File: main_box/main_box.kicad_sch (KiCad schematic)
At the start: 0 parts

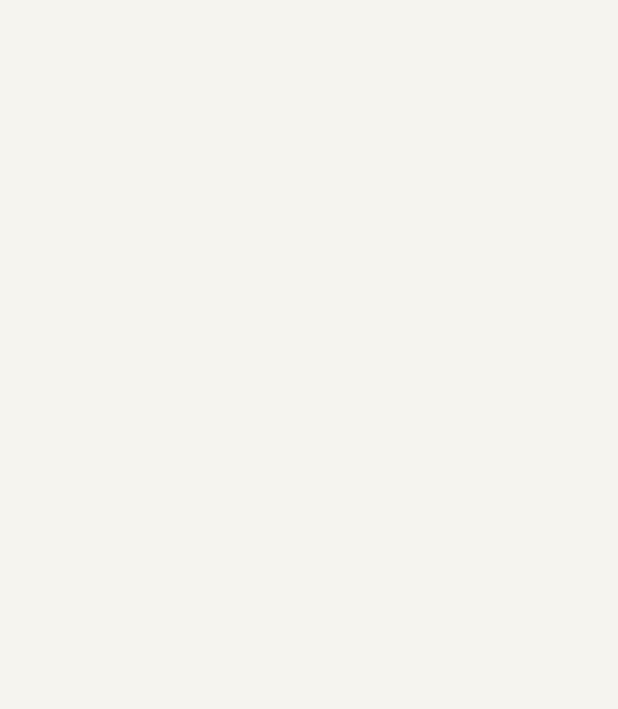
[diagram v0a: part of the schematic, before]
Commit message: Added 5v pówer supply for independent raspberry pi power, modified the switchgear topology
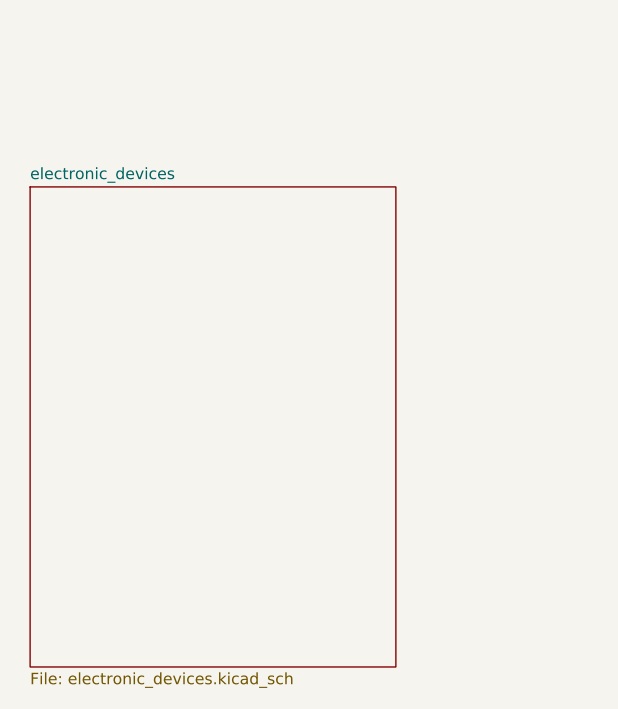
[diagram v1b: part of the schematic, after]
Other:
- added sheet electronic_devices (electronic_devices.kicad_sch)
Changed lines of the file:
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@@
+    )
+  )
+  (sheet (at 22.86 102.87) (size 40.64 53.34) (fields_autoplaced)
+    (stroke (width 0.1524) (type solid) (color 0 0 0 0))
+    (fill (color 0 0 0 0.0000))
+    (property "Sheet name" "electronic_devices" (id 0) (at 22.86 102.1584 0)
+      (effects (font (size 1.27 1.27)) (justify left bottom))
+    )
+    (property "Sheet file" "electronic_devices.kicad_sch" (id 1) (at 22.86 156.7946 0)
+      (effects (font (size 1.27 1.27)) (justify left top))
     )
   )
@@
     (path "/7bafe9bc-eba9-4810-a855-8b4f34bb53ef" (page "3"))
     (path "/63d2de20-f243-448e-8f9b-9238fd5af361" (page "4"))
+    (path "/eb51af8c-f931-4087-841b-b930618e5f3f" (page "5"))
+  )
+  (symbol_instances
+    (path "/63d2de20-f243-448e-8f9b-9238fd5af361/2175fe63-e824-4590-bc28-3e8589ee19d9"
+      (reference "#PWR?") (unit 1) (value "+48V") (footprint "")
+    )
+    (path "/997c2f12-73ba-4c01-9ee0-42e37cbab790/4d0b4730-b3d1-43cb-accd-4cc79974c8c5"
+      (reference "#PWR?") (unit 1) (value "AC") (footprint "")
+    )
+    (path "/63d2de20-f243-448e-8f9b-9238fd5af361/68c81a5f-fa55-4394-b81b-8e4332a2bcfc"
+      (reference "#PWR?") (unit 1) (value "GND") (footprint "")
+    )
+    (path "/63d2de20-f243-448e-8f9b-9238fd5af361/726d0c38-9170-4a3a-b0d1-f86487597b7c"
+      (reference "#PWR?") (unit 1) (value "~") (footprint "")
+    )
+    (path "/997c2f12-73ba-4c01-9ee0-42e37cbab790/8dd2ebd0-beab-4a6a-a970-4109d2d0d2a4"
+      (reference "#PWR?") (unit 1) (value "+48V") (footprint "")
+    )
+    (path "/997c2f12-73ba-4c01-9ee0-42e37cbab790/c7b12abe-ed41-4f50-ac10-dd4835ba4d6b"
+      (reference "#PWR?") (unit 1) (value "NEUT") (footprint "")
+    )
+    (path "/63d2de20-f243-448e-8f9b-9238fd5af361/d406e969-3bf2-4103-82ab-fd8afd1ab904"
+      (reference "#PWR?") (unit 1) (value "+12V") (footprint "")
+    )
+    (path "/997c2f12-73ba-4c01-9ee0-42e37cbab790/5a4ab1af-60d4-416e-8b38-9da9038b6357"
+      (reference "CB?") (unit 1) (value "differential_2P") (footprint "")
+    )
+    (path "/7bafe9bc-eba9-4810-a855-8b4f34bb53ef/8a76ef98-e96c-4d23-a378-4cc52811dfea"
+      (reference "CB?") (unit 1) (value "CircuitBreaker_1P") (footprint "")
+    )
+    (path "/997c2f12-73ba-4c01-9ee0-42e37cbab790/b31f38ac-b940-4846-9b48-43ebbd4f4b50"
+      (reference "CB?") (unit 1) (value "CircuitBreaker_1P") (footprint "")
+    )
+    (path "/7bafe9bc-eba9-4810-a855-8b4f34bb53ef/bf176895-6463-4f0f-9592-ff4d9d0b2b75"
+      (reference "CB?") (unit 1) (value "CircuitBreaker_1P") (footprint "")
+    )
+    (path "/63d2de20-f243-448e-8f9b-9238fd5af361/392a6c81-87bf-462f-ae4f-8f6cff061eac"
+      (reference "DB?") (unit 1) (value "~") (footprint "")
+    )
+    (path "/63d2de20-f243-448e-8f9b-9238fd5af361/d6dbef17-62e8-4d1a-ae5f-76ffe5d4c965"
+      (reference "DB?") (unit 1) (value "~") (footprint "")
+    )
+    (path "/63d2de20-f243-448e-8f9b-9238fd5af361/06522ea9-d173-4338-bd32-16c7972a5738"
+      (reference "DB?") (unit 2) (value "~") (footprint "")
+    )
+    (path "/63d2de20-f243-448e-8f9b-9238fd5af361/9757504d-09cf-42ef-8a09-75a534971024"
+      (reference "DB?") (unit 2) (value "~") (footprint "")
+    )
+    (path "/63d2de20-f243-448e-8f9b-9238fd5af361/ab507e4e-003b-4535-b07f-485a6ae64fc2"
+      (reference "DB?") (unit 3) (value "~") (footprint "")
+    )
+    (path "/63d2de20-f243-448e-8f9b-9238fd5af361/e4e9a9cd-894c-43a6-bbd2-9190e99d71d4"
+      (reference "DB?") (unit 3) (value "~") (footprint "")
+    )
+    (path "/63d2de20-f243-448e-8f9b-9238fd5af361/60441c07-2cfe-4ab7-8123-6ac0d5286bab"
+      (reference "DB?") (unit 4) (value "~") (footprint "")
+    )
+    (path "/63d2de20-f243-448e-8f9b-9238fd5af361/e0865ab7-e95c-4d84-b2ee-1110789115aa"
+      (reference "DB?") (unit 4) (value "~") (footprint "")
+    )
+    (path "/7bafe9bc-eba9-4810-a855-8b4f34bb53ef/d1fd7aa5-fc44-43fd-ad27-c11c494acc16"
+      (reference "KM?") (unit 1) (value "~") (footprint "")
+    )
+    (path "/7bafe9bc-eba9-4810-a855-8b4f34bb53ef/d20f544e-c1b7-4c1b-ad40-4ad7e6dfd1e9"
+      (reference "LA?") (unit 1) (value "~") (footprint "")
+    )
+    (path "/7bafe9bc-eba9-4810-a855-8b4f34bb53ef/f0158284-f11f-4236-9b56-2a100def7c5c"
+      (reference "LA?") (unit 1) (value "~") (footprint "")
+    )
+    (path "/997c2f12-73ba-4c01-9ee0-42e37cbab790/a852d65e-5762-4110-8194-84b1a09544cf"
+      (reference "PS?") (unit 1) (value "~") (footprint "")
+    )
+    (path "/997c2f12-73ba-4c01-9ee0-42e37cbab790/b8c86405-bc7a-4b8c-843a-d54bddee4e0f"
+      (reference "PS?") (unit 1) (value "power_suppy") (footprint "")
+    )
+    (path "/7bafe9bc-eba9-4810-a855-8b4f34bb53ef/4aa64336-d125-4fcd-ab28-2935cd4f1752"
+      (reference "TB?") (unit 1) (value "~") (footprint "")
+    )
+    (path "/7bafe9bc-eba9-4810-a855-8b4f34bb53ef/bce5b1ac-044e-4b74-9db6-acb90b2d00f2"
+      (reference "TB?") (unit 1) (value "terminal_block_single") (footprint "")
+    )
   )
 )
